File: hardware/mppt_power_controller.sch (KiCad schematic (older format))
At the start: 60 parts, among them J1 Solar Input, J2 USB_B_Micro, J3 Conn_ARM_JTAG_SWD_10, J4 Battery, J5 Curiosity Board, Q1 Q_NMOS_GSD, Q2 Q_NMOS_GSD, U1 INA233, U2 PX3519, U3 ATSAMD21G18A-AUT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

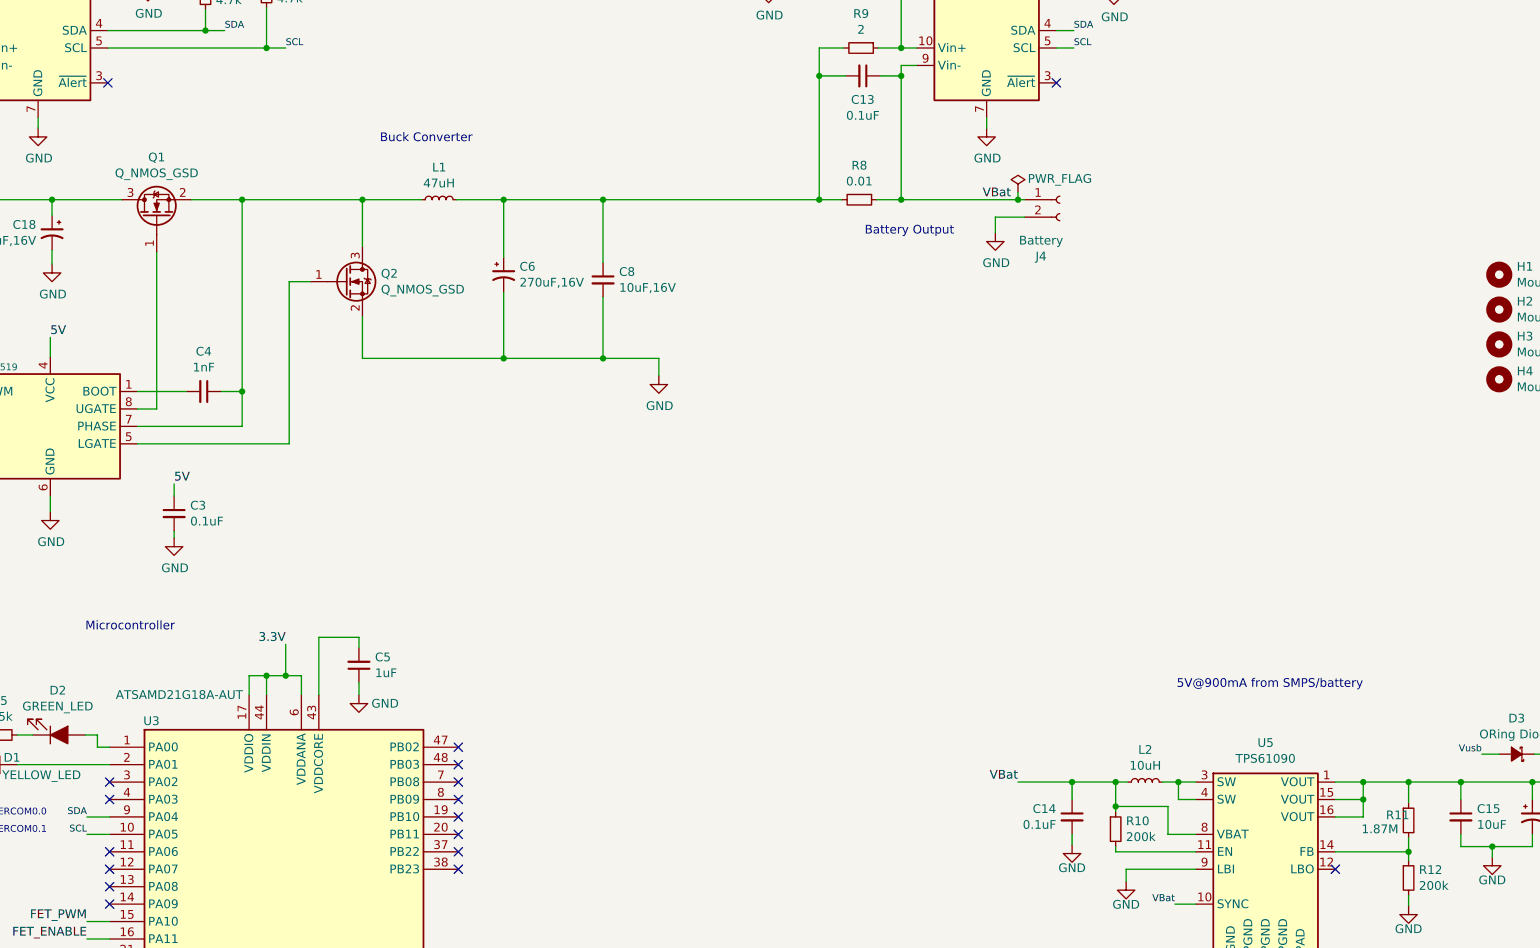
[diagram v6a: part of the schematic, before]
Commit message: Add a test point for VBat. Route rest of power, I2C, test points, and everything else! Lots of cleanup needed from here to make the board look nice, but all of the nets have been routed.
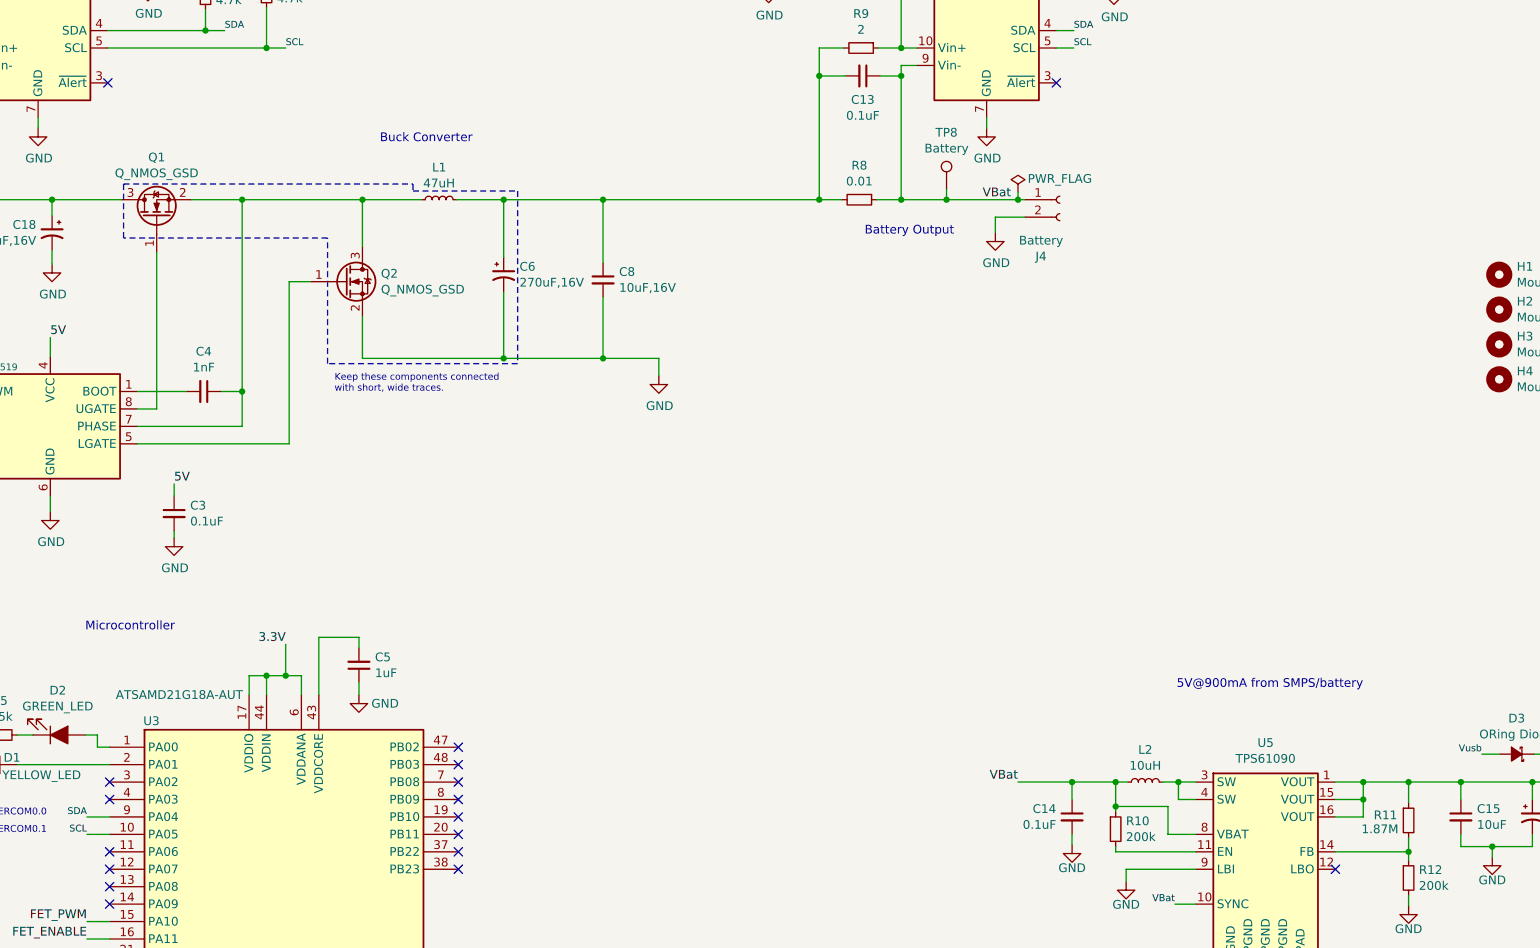
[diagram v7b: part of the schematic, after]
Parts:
- added TP8: Battery, TestPoint:TestPoint_Keystone_5019_Minature, symbol Connector:TestPoint
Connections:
- net VBat: now also TP8.1
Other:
- note added: "Keep these components connected\nwith short, wide traces."
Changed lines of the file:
@@
 U 1 1 5DAD26E1
 P 11480 6730
-F 0 "R11" H 11350 6760 50  0000 L CNN
+F 0 "R11" H 11280 6760 50  0000 L CNN
 F 1 "1.87M" H 11210 6680 50  0000 L CNN
 F 2 "Resistor_SMD:R_0603_1608Metric_Pad1.05x0.95mm_HandSolder" H 11480 6730 50  0001 C CNN
@@
 	8430 3170 8570 3170
 Wire Wire Line
-	8570 3170 9240 3170
+	8570 3170 8830 3170
 Connection ~ 8570 3170
 NoConn ~ 9460 2500
@@
 Text Label 3900 7410 2    50   ~ 0
 FET_ENABLE
-$Comp
-L Connector:TestPoint TP3
-U 1 1 5DB2BA0C
-P 13400 1950
-F 0 "TP3" H 13458 2068 50  0000 L CNN
-F 1 "SDA" H 13458 1977 50  0000 L CNN
-F 2 "TestPoint:TestPoint_Keystone_5019_Minature" H 13600 1950 50  0001 C CNN
-F 3 "~" H 13600 1950 50  0001 C CNN
-F 4 "Keystone 5019" H 13400 1950 50  0001 C CNN "P/N"
-	1    13400 1950
-	1    0    0    -1
-$EndComp
-$Comp
-L Connector:TestPoint TP4
-U 1 1 5DB2D1C2
-P 13670 1950
-F 0 "TP4" H 13728 2068 50  0000 L CNN
-F 1 "SCL" H 13728 1977 50  0000 L CNN
-F 2 "TestPoint:TestPoint_Keystone_5019_Minature" H 13870 1950 50  0001 C CNN
-F 3 "~" H 13870 1950 50  0001 C CNN
-F 4 "Keystone 5019" H 13670 1950 50  0001 C CNN "P/N"
-	1    13670 1950
-	1    0    0    -1
-$EndComp
-$Comp
-L Connector:TestPoint TP5
-U 1 1 5DB2D5E3
-P 13950 1950
-F 0 "TP5" H 14008 2068 50  0000 L CNN
-F 1 "5V" H 14008 1977 50  0000 L CNN
-F 2 "TestPoint:TestPoint_Keystone_5019_Minature" H 14150 1950 50  0001 C CNN
-F 3 "~" H 14150 1950 50  0001 C CNN
-F 4 "Keystone 5019" H 13950 1950 50  0001 C CNN "P/N"
-	1    13950 1950
-	1    0    0    -1
-$EndComp
-$Comp
-L Connector:TestPoint TP6
-U 1 1 5DB2D95C
-P 14220 1950
-F 0 "TP6" H 14278 2068 50  0000 L CNN
-F 1 "3.3V" H 14278 1977 50  0000 L CNN
-F 2 "TestPoint:TestPoint_Keystone_5019_Minature" H 14420 1950 50  0001 C CNN
-F 3 "~" H 14420 1950 50  0001 C CNN
-F 4 "Keystone 5019" H 14220 1950 50  0001 C CNN "P/N"
-	1    14220 1950
-	1    0    0    -1
-$EndComp
-$Comp
-L Connector:TestPoint TP7
-U 1 1 5DB2DC57
-P 14510 1950
-F 0 "TP7" H 14568 2068 50  0000 L CNN
-F 1 "GND" H 14568 1977 50  0000 L CNN
-F 2 "TestPoint:TestPoint_Keystone_5019_Minature" H 14710 1950 50  0001 C CNN
-F 3 "~" H 14710 1950 50  0001 C CNN
-F 4 "Keystone 5019" H 14510 1950 50  0001 C CNN "P/N"
-	1    14510 1950
-	1    0    0    -1
-$EndComp
 Wire Wire Line
 	13400 2000 13400 1950
@@
 	14510 2400 14510 1950
 Connection ~ 13300 2400
-$Comp
-L Connector:TestPoint TP1
-U 1 1 5DB2E7FF
-P 1560 3110
-F 0 "TP1" H 1618 3228 50  0000 L CNN
-F 1 "Solar" H 1618 3137 50  0000 L CNN
-F 2 "TestPoint:TestPoint_Keystone_5019_Minature" H 1760 3110 50  0001 C CNN
-F 3 "~" H 1760 3110 50  0001 C CNN
-F 4 "Keystone 5019" H 1560 3110 50  0001 C CNN "P/N"
-	1    1560 3110
-	1    0    0    -1
-$EndComp
 Wire Wire Line
 	1560 3110 1560 3170
@@
 	1550 3270 1550 3370
 $Comp
-L power:GND #PWR?
+L power:GND #PWR026
 U 1 1 5DB30CA4
 P 3700 3540
-F 0 "#PWR?" H 3700 3290 50  0001 C CNN
+F 0 "#PWR026" H 3700 3290 50  0001 C CNN
 F 1 "GND" H 3705 3367 50  0000 C CNN
 F 2 "" H 3700 3540 50  0001 C CNN
@@
 Wire Wire Line
 	3700 3170 4100 3170
+Wire Notes Line
+	5770 3080 5770 3120
+Wire Notes Line
+	5770 3120 6370 3120
+Wire Notes Line
+	6370 3120 6370 4110
+Wire Notes Line
+	6370 4110 5280 4110
+Wire Notes Line
+	5280 4110 5280 3390
+Wire Notes Line
+	5280 3390 4110 3390
+Wire Notes Line
+	4110 3390 4110 3080
+Wire Notes Line
+	4110 3080 5770 3080
+Text Notes 5320 4280 0    39   ~ 0
+Keep these components connected\nwith short, wide traces.
+Wire Wire Line
+	8830 3110 8830 3170
+Connection ~ 8830 3170
+Wire Wire Line
+	8830 3170 9240 3170
+$Comp
+L Connector:TestPoint TP7
+U 1 1 5DB2DC57
+P 14510 1950
+F 0 "TP7" H 14568 2068 50  0000 L CNN
+F 1 "GND" H 14568 1977 50  0000 L CNN
+F 2 "TestPoint:TestPoint_Keystone_5019_Minature" H 14710 1950 50  0001 C CNN
+F 3 "~" H 14710 1950 50  0001 C CNN
+F 4 "Keystone 5019" H 14510 1950 50  0001 C CNN "P/N"
+	1    14510 1950
+	1    0    0    -1
+$EndComp
+$Comp
+L Connector:TestPoint TP6
+U 1 1 5DB2D95C
+P 14220 1950
+F 0 "TP6" H 14278 2068 50  0000 L CNN
+F 1 "3.3V" H 14278 1977 50  0000 L CNN
+F 2 "TestPoint:TestPoint_Keystone_5019_Minature" H 14420 1950 50  0001 C CNN
+F 3 "~" H 14420 1950 50  0001 C CNN
+F 4 "Keystone 5019" H 14220 1950 50  0001 C CNN "P/N"
+	1    14220 1950
+	1    0    0    -1
+$EndComp
+$Comp
+L Connector:TestPoint TP5
+U 1 1 5DB2D5E3
+P 13950 1950
+F 0 "TP5" H 14008 2068 50  0000 L CNN
+F 1 "5V" H 14008 1977 50  0000 L CNN
+F 2 "TestPoint:TestPoint_Keystone_5019_Minature" H 14150 1950 50  0001 C CNN
+F 3 "~" H 14150 1950 50  0001 C CNN
+F 4 "Keystone 5019" H 13950 1950 50  0001 C CNN "P/N"
+	1    13950 1950
+	1    0    0    -1
+$EndComp
+$Comp
+L Connector:TestPoint TP4
+U 1 1 5DB2D1C2
+P 13670 1950
+F 0 "TP4" H 13728 2068 50  0000 L CNN
+F 1 "SCL" H 13728 1977 50  0000 L CNN
+F 2 "TestPoint:TestPoint_Keystone_5019_Minature" H 13870 1950 50  0001 C CNN
+F 3 "~" H 13870 1950 50  0001 C CNN
+F 4 "Keystone 5019" H 13670 1950 50  0001 C CNN "P/N"
+	1    13670 1950
+	1    0    0    -1
+$EndComp
+$Comp
+L Connector:TestPoint TP3
+U 1 1 5DB2BA0C
+P 13400 1950
+F 0 "TP3" H 13458 2068 50  0000 L CNN
+F 1 "SDA" H 13458 1977 50  0000 L CNN
+F 2 "TestPoint:TestPoint_Keystone_5019_Minature" H 13600 1950 50  0001 C CNN
+F 3 "~" H 13600 1950 50  0001 C CNN
+F 4 "Keystone 5019" H 13400 1950 50  0001 C CNN "P/N"
+	1    13400 1950
+	1    0    0    -1
+$EndComp
+$Comp
+L Connector:TestPoint TP1
+U 1 1 5DB2E7FF
+P 1560 3110
+F 0 "TP1" H 1618 3228 50  0000 L CNN
+F 1 "Solar" H 1618 3137 50  0000 L CNN
+F 2 "TestPoint:TestPoint_Keystone_5019_Minature" H 1760 3110 50  0001 C CNN
+F 3 "~" H 1760 3110 50  0001 C CNN
+F 4 "Keystone 5019" H 1560 3110 50  0001 C CNN "P/N"
+	1    1560 3110
+	1    0    0    -1
+$EndComp
+$Comp
+L Connector:TestPoint TP8
+U 1 1 5DBCB834
+P 8830 3110
+F 0 "TP8" H 8830 3435 50  0000 C CNN
+F 1 "Battery" H 8830 3344 50  0000 C CNN
+F 2 "TestPoint:TestPoint_Keystone_5019_Minature" H 9030 3110 50  0001 C CNN
+F 3 "~" H 9030 3110 50  0001 C CNN
+F 4 "Keystone 5019" H 8830 3110 50  0001 C CNN "P/N"
+	1    8830 3110
+	1    0    0    -1
+$EndComp
 $EndSCHEMATC

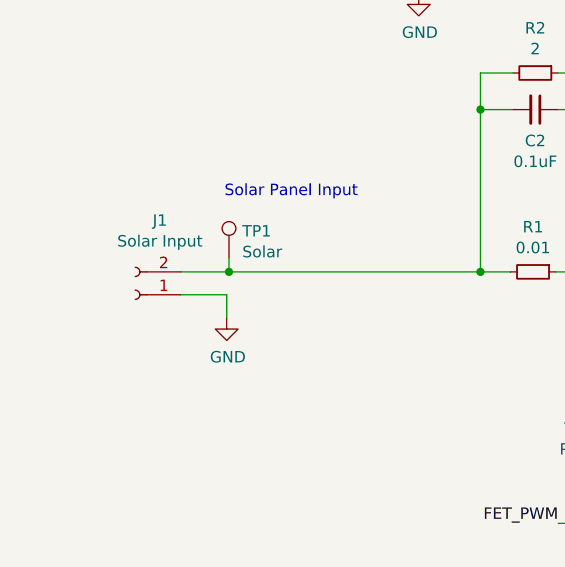
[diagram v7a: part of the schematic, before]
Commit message: Flip solar panel connector around so pin 1 is power and pin 2 is ground like every other board with JST connectors.
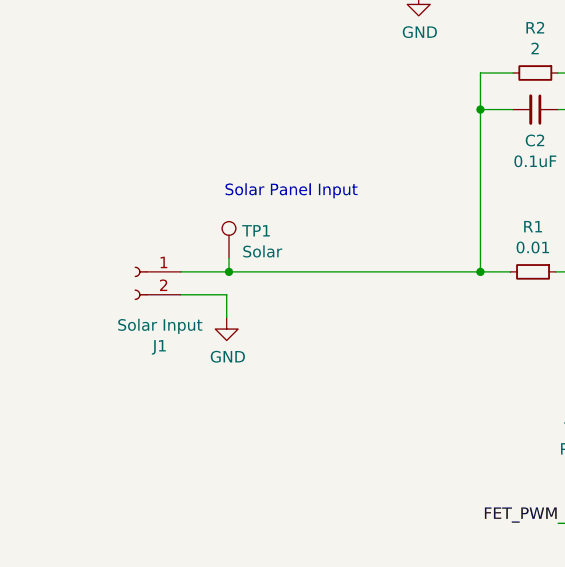
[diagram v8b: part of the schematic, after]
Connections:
- net GND: now also J1.2 (Pin_2); no longer J1.1 (Pin_1)
- net at C2.2, R1.2, R2.2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: now also J1.1 (Pin_1); no longer J1.2 (Pin_2)
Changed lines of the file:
@@
 L Connector:Conn_01x02_Female J1
 U 1 1 5DAA0A41
-P 1150 3270
-F 0 "J1" H 1042 2945 50  0000 C CNN
-F 1 "Solar Input" H 1042 3036 50  0000 C CNN
-F 2 "Connector_JST:JST_PH_S2B-PH-K_1x02_P2.00mm_Horizontal" H 1150 3270 50  0001 C CNN
-F 3 "~" H 1150 3270 50  0001 C CNN
-	1    1150 3270
-	-1   0    0    1
+P 1150 3170
+F 0 "J1" H 1042 2845 50  0000 C CNN
+F 1 "Solar Input" H 1042 2936 50  0000 C CNN
+F 2 "Connector_JST:JST_PH_S2B-PH-K_1x02_P2.00mm_Horizontal" H 1150 3170 50  0001 C CNN
+F 3 "~" H 1150 3170 50  0001 C CNN
+	1    1150 3170
+	-1   0    0    -1
 $EndComp
 $Comp
